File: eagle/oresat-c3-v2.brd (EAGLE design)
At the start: 99.8 x 94.7 mm, 168 parts, among them J1 J-SAMTEC-TFM-110-X1-XXX-D-RA, J10 U.FL, J11 U.FL, J13 U.FL, J14 U.FL, J15 HARWIN-2X8X1.27, J19 HARWIN-2X8X1.27, J2 U.FL, J3 U.FL, J4 U.FL, J6 J-SAMTEC-TFM-120-X1-XXX-D-RA, J7 FTSH-105-XX-X-DV-K, J8 U.FL, J9 U.FL, Q1 MOSFET-PCH-SOT23-6, U1 MAX892LEUA+T21-0036K-L, U11 U-ONSEMI-AX5043, U12 LP2985XX-N, U13 U-ONSEMI-AX5043, U14 LP2985XX-N, U2 TCAN330, U3 TCAN330, U4 TPS259621 - eFuse, U5 TPS62111RSA, U6 MAX6374KA-T21-0078H-L, U7 STM32F446RE, U9 SFEM016GB1EM1TO-A-HG-111-STD, X1 16MHZ-2.5x2mm, X3 TAITIEN-TY, X4 TAITIEN-TY

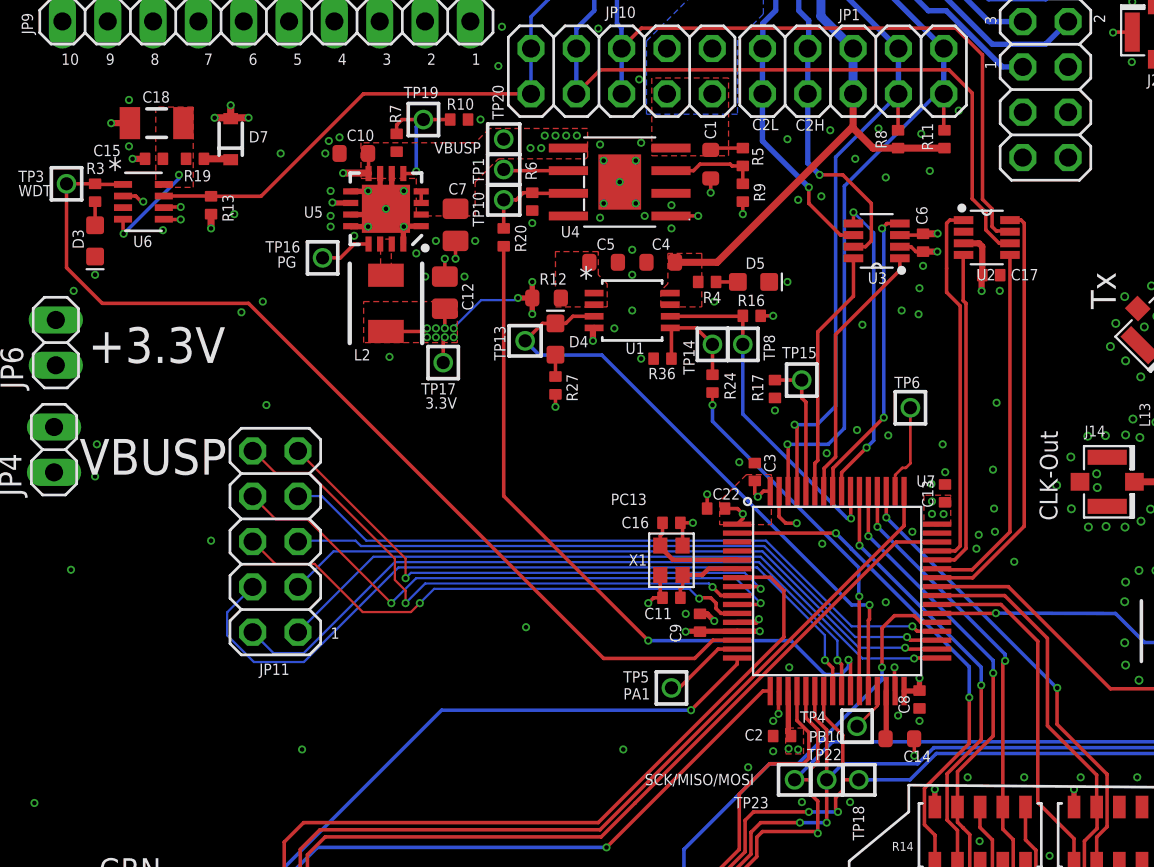
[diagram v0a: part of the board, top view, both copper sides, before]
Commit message: Replacing non 0603 with 0603 package equivalents
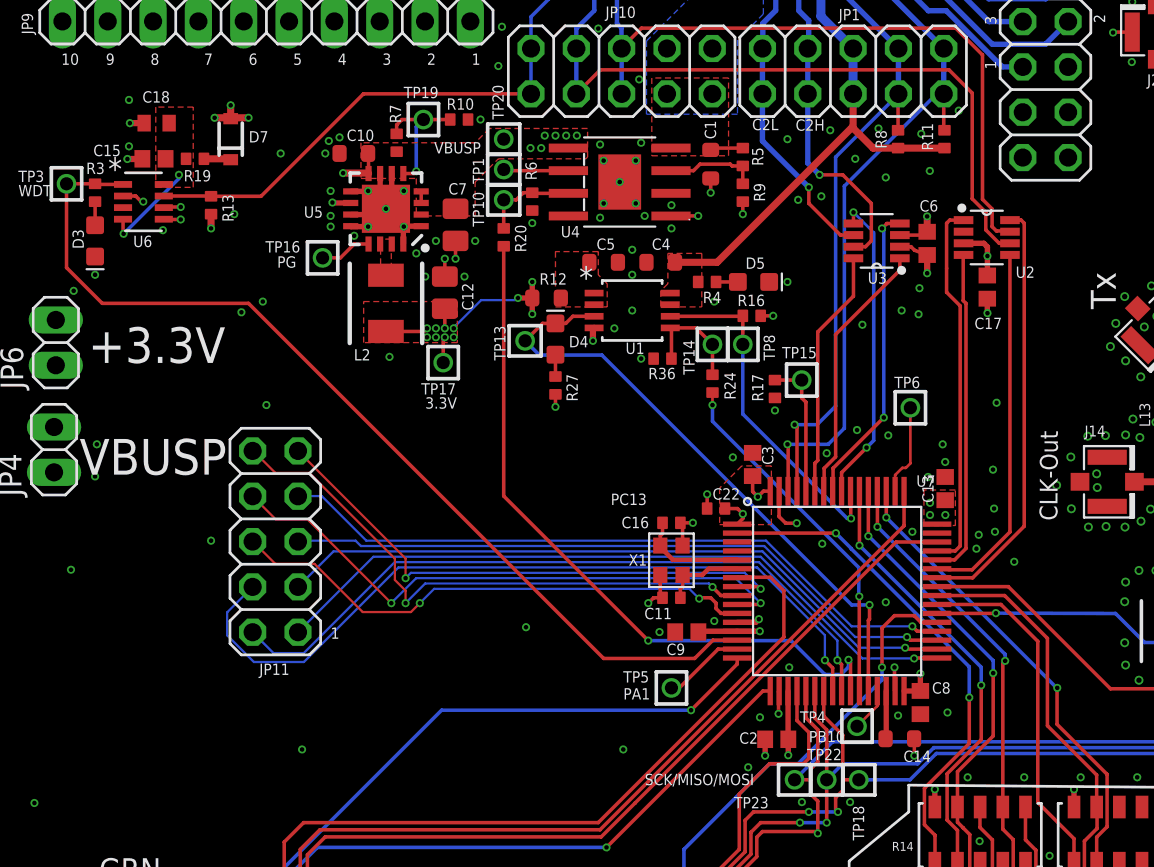
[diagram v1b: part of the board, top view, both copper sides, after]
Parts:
- C13, C15, C17, C2, C3, C6, C8, C9: device oresat-rcl:.0402-B-NOSILK -> SamacSys_Parts:CAPC1608X95N
- C18: device oresat-rcl:1206-B -> SamacSys_Parts:CAPC1608X90N
- moved C9 0.90 mm to (45.6, 48.6), turned to 0 degrees
- moved C17 0.71 mm to (62.4, 67.9), turned to 90 degrees
- moved C3 0.44 mm to (49.2, 58.0)
- moved C2 0.35 mm to (50.6, 42.6)
- moved C13 0.27 mm to (60.0, 56.6)
- moved C6 0.23 mm to (59.0, 70.4)
- moved C8 0.18 mm to (58.6, 44.6)
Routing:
- net GND: track 107.0 -> 108.2 mm, vias 507 -> 506
- net 3.3V: track 56.9 -> 57.6 mm, vias 45 -> 43

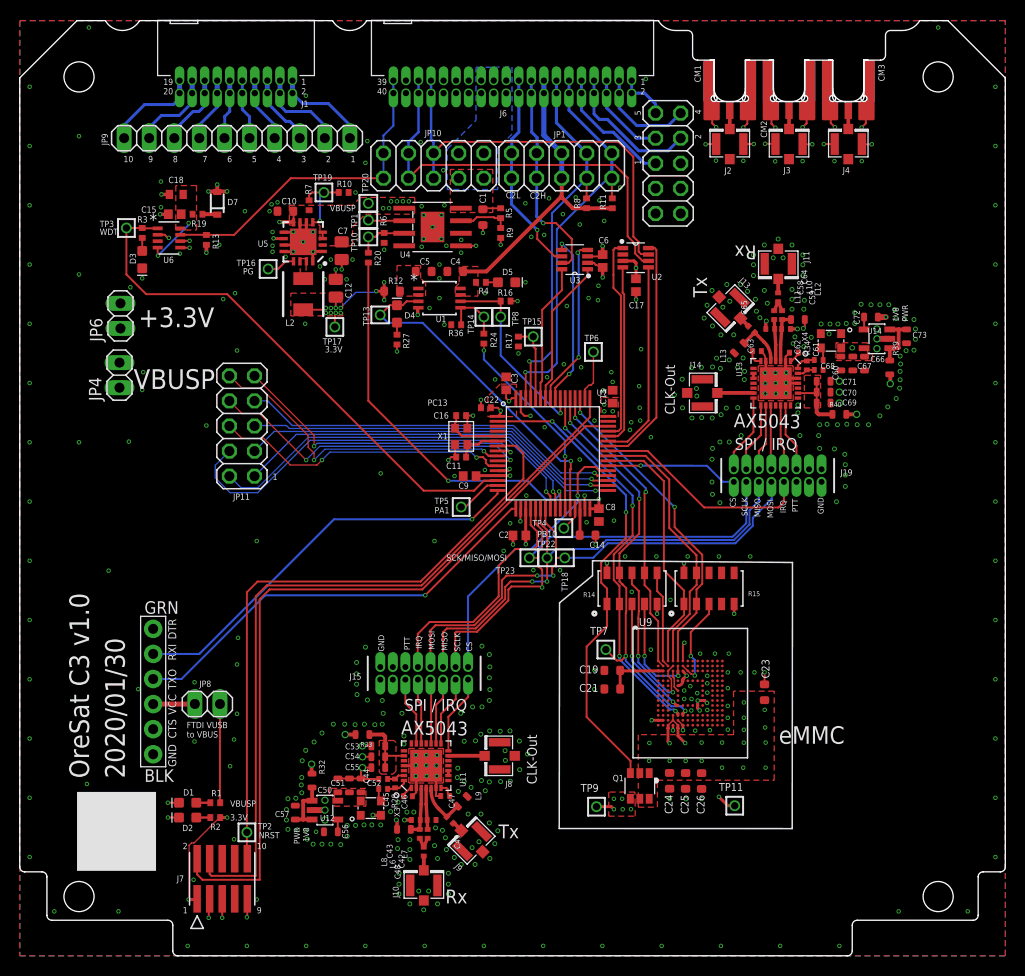
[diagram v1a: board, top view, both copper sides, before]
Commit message: Replaced non 0603 passive components with available 0603 equivalents
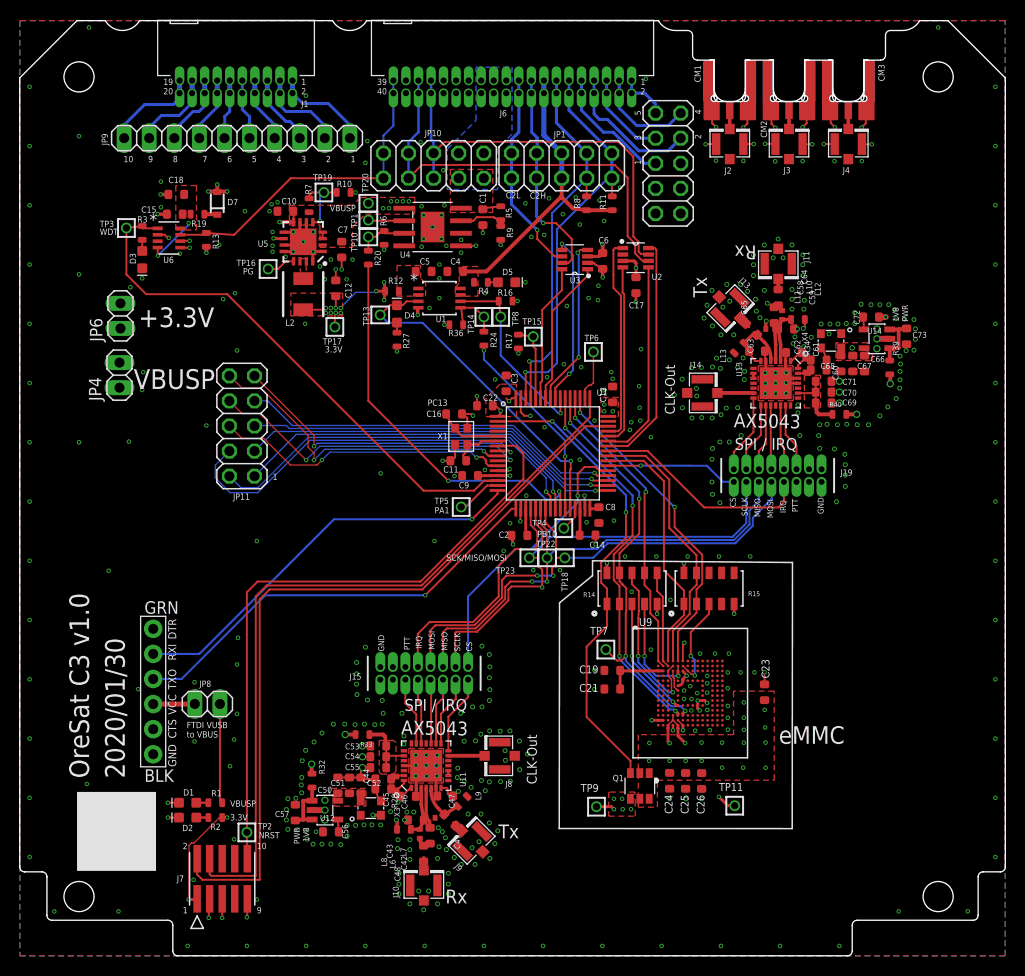
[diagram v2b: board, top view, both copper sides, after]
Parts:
- C1, C23, C24, C25, C4, C5: value 1u -> 1uF; device oresat-rcl:.0603-B-NOSILK -> C3_SamacSys_Parts:.0603-B-NOSILK
- C10: value 1u -> 10uF; device oresat-rcl:.0603-B-NOSILK -> C3_SamacSys_Parts:.0603-B-NOSILK
- C11: value 20p -> 20pF; device rcl_custom:.0402-B-NOSILK -> C3_SamacSys_Parts:.0603-B-NOSILK
- C12: value 22u -> 22pF; device oresat-rcl:.0805-B-NOSILK -> C3_SamacSys_Parts:.0603-B-NOSILK
- C13, C15, C17, C2, C3, C6, C8, C9: value 100n -> 0.1uf; device SamacSys_Parts:CAPC1608X95N -> C3_SamacSys_Parts:.0603-B-NOSILK
- C14: value 2.2u -> 2.2uF; device oresat-rcl:.0603-B-NOSILK -> C3_SamacSys_Parts:.0603-B-NOSILK
- C16: value 20p -> 20pF; device oresat-rcl:.0402-B-NOSILK -> C3_SamacSys_Parts:.0603-B-NOSILK
- C18: value 47u -> 47uF; device SamacSys_Parts:CAPC1608X90N -> C3_SamacSys_Parts:.0603-B-NOSILK
- C19, C26: device oresat-rcl:.0603-B-NOSILK -> C3_SamacSys_Parts:.0603-B-NOSILK
- C21: value 0.1u -> 0.1uf; device oresat-rcl:.0603-B-NOSILK -> C3_SamacSys_Parts:.0603-B-NOSILK
- C22: value 100n -> 0.1uf; device oresat-rcl:.0402-B-NOSILK -> C3_SamacSys_Parts:.0603-B-NOSILK
- C42, C43, C58, C59: value 8.2p -> 8.2pF; device oresat-rcl:.0402-C-NOSILK -> C3_SamacSys_Parts:.0603-B-NOSILK
- C44, C45, C60, C61: value 1n -> 1000pF; device oresat-rcl:.0402-C-NOSILK -> C3_SamacSys_Parts:.0603-B-NOSILK
- C46, C47, C62, C63: value 82p -> 82pF; device oresat-rcl:.0402-C-NOSILK -> C3_SamacSys_Parts:.0603-B-NOSILK
- C48, C49, C64, C65: value 22p -> 22pF; device oresat-rcl:.0402-C-NOSILK -> C3_SamacSys_Parts:.0603-B-NOSILK
- C50, C53, C66, C69: value 22n -> 0.022uF; device oresat-rcl:.0603-C-NOSILK -> C3_SamacSys_Parts:.0603-B-NOSILK
- C51, C54: value NP -> 0.022uF; device oresat-rcl:.0603-C-NOSILK -> C3_SamacSys_Parts:.0603-B-NOSILK
- C52, C55, C68, C71: value 4.7u -> 4.7uF; device oresat-rcl:.0603-C-NOSILK -> C3_SamacSys_Parts:.0603-B-NOSILK
- C56, C72: device oresat-rcl:.0603-C-NOSILK -> C3_SamacSys_Parts:.0603-B-NOSILK
- C57, C73: value 1u -> 1uF; device oresat-rcl:.0603-C-NOSILK -> C3_SamacSys_Parts:.0603-B-NOSILK
- C67, C70: value NP -> 0.1uf; device oresat-rcl:.0603-C-NOSILK -> C3_SamacSys_Parts:.0603-B-NOSILK
- C7: value 10u -> 10uF; device oresat-rcl:.0805-B-NOSILK -> C3_SamacSys_Parts:.0603-B-NOSILK
- R1, R10, R11, R13, R16, R17, R19, R2, R20, R24, R27, R3, R4, R6, R7, R8, R9: device oresat-rcl:.0402-B-NOSILK -> C3_SamacSys_Parts:.0603-C-NOSILK
- R12: device oresat-rcl:.0603-B-NOSILK -> C3_SamacSys_Parts:.0603-C-NOSILK
- R28, R34: device oresat-rcl:.0402-C-NOSILK -> C3_SamacSys_Parts:.0603-C-NOSILK
- R32, R33, R39, R40: device oresat-rcl:.0603-C-NOSILK -> C3_SamacSys_Parts:.0603-C-NOSILK
- R36: value 23.9k -> 23.7k; device oresat-rcl:.0402-B-NOSILK -> C3_SamacSys_Parts:.0603-C-NOSILK
- R5: value 31.7k -> 31.6k; device oresat-rcl:.0402-B-NOSILK -> C3_SamacSys_Parts:.0603-C-NOSILK
- moved C16 0.74 mm to (44.0, 54.9)
- moved C11 0.47 mm to (44.4, 50.1)
- moved C42 0.31 mm to (41.6, 12.2)
- moved L7 0.24 mm to (41.6, 14.0)
- moved C13 0.23 mm to (60.0, 56.9)
- moved C22 0.22 mm to (47.1, 55.7)
- moved C48 0.21 mm to (40.9, 10.3)
- moved C7 0.12 mm to (32.6, 71.5)
- moved C9 0.06 mm to (45.6, 48.6)
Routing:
- net 3.3V: track 57.6 -> 54.1 mm, vias 43 -> 41
- net N$17: track 1.97 -> 1.13 mm
- net CRYSTALOUT: track 4.53 -> 5.13 mm

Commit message: Parts Move so far
not completed
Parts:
- removed JP11, JP2: (no value), pinhead:2X05
- removed JP4, JP6: (no value), J-2X8X1.27:1X02
- removed TP9: TEST-POINT, Tova:2MM-TEST-POINT
- moved TP11 72.5 mm to (7.29, 47.1)
- moved C26 67.7 mm to (9.10, 49.1), turned to 180 degrees
- moved C25 67.0 mm to (9.11, 50.7), turned to 180 degrees
- moved C24 66.4 mm to (9.12, 52.4), turned to 180 degrees
- moved C23 59.5 mm to (18.1, 42.8), turned to 0 degrees
- moved D2 58.0 mm to (20.0, 71.9)
- moved R2 58.0 mm to (22.8, 71.9)
- moved D1 57.9 mm to (20.1, 73.3)
- moved R1 57.9 mm to (22.9, 73.3)
- moved U9 55.2 mm to (18.0, 50.3), turned to 270 degrees
- moved Q1 54.9 mm to (13.9, 42.1), turned to 270 degrees
- moved C21 52.0 mm to (18.4, 58.2), turned to 90 degrees
- moved C19 49.3 mm to (20.3, 58.2), turned to 90 degrees
- moved TP7 47.7 mm to (22.1, 60.7)
- moved R15 42.7 mm to (28.6, 48.4), turned to 0 degrees
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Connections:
- net !SD renamed SD
- removed net SPARE1: J6.10, J6.9, JP2.5
- removed net SPARE2: J6.7, J6.8, JP2.4
- removed net SPARE3: J6.5, J6.6, JP2.3
- removed net SPARE4: J6.3, J6.4, JP2.2
- removed net SPARE5: J6.1, J6.2, JP2.1
- net 3.3V: no longer JP6.1, JP6.2, TP9.1
- net GND: no longer JP2.10, JP2.7, JP2.8, JP2.9
- net MMC_PWR: now also R15.6; no longer R14.1
- net PB12: no longer JP11.1
- net PC0: no longer JP11.9
- net PC1: no longer JP11.10
- net PC2: no longer JP11.8
- net PC3: no longer JP11.6
- net PC4: no longer JP11.4
- net PC5: no longer JP11.2
- net SDIO_CK: now also R14.2; no longer R14.9
- net SDIO_CMD: now also R14.9; no longer R14.2
- net SPI2_MISO: no longer JP11.5
- net SPI2_MOSI: no longer JP11.7
- net SPI2_SCK: no longer JP11.3
- net VBUSP: no longer JP4.1, JP4.2
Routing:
- net VBUSP: track 74.5 -> 1.95 mm, vias 7 -> 6
- net SWCLK: track 77.9 -> 22.2 mm, vias 0 -> 2
- net SWDIO: track 79.1 -> 27.5 mm, vias 0 -> 2
- net NRST: track 65.3 -> 14.9 mm, vias 0 -> 2
- net PC4: track 44.5 -> 0.00 mm, vias 1 -> 0
- net USART2_RX: track 43.9 -> 0.00 mm, vias 1 -> 0
- net SPI1_MOSI: track 53.6 -> 10.9 mm, vias 2 -> 0
- net USART2_TX: track 41.9 -> 0.00 mm, vias 1 -> 0
- net SPI1_MISO: track 51.2 -> 10.6 mm, vias 2 -> 0
- net SPI1_SCK: track 51.9 -> 11.5 mm, vias 1 -> 0
- net PC5: track 40.1 -> 0.00 mm, vias 1 -> 0
- net PB12: track 39.9 -> 0.00 mm, vias 1 -> 0
- net CB_IOUT_IN: track 39.7 -> 0.00 mm, vias 2 -> 0
- net SPI2_MOSI: track 39.0 -> 0.00 mm, vias 1 -> 0
- net SPI2_SCK: track 38.9 -> 0.00 mm, vias 1 -> 0
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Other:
- board text added: "BOOT0"
- board text added: "SDIO_CK"
- board text removed: "+3.3V"
- board text removed: "PC13"
- board text removed: "SCK/MISO/MOSI"

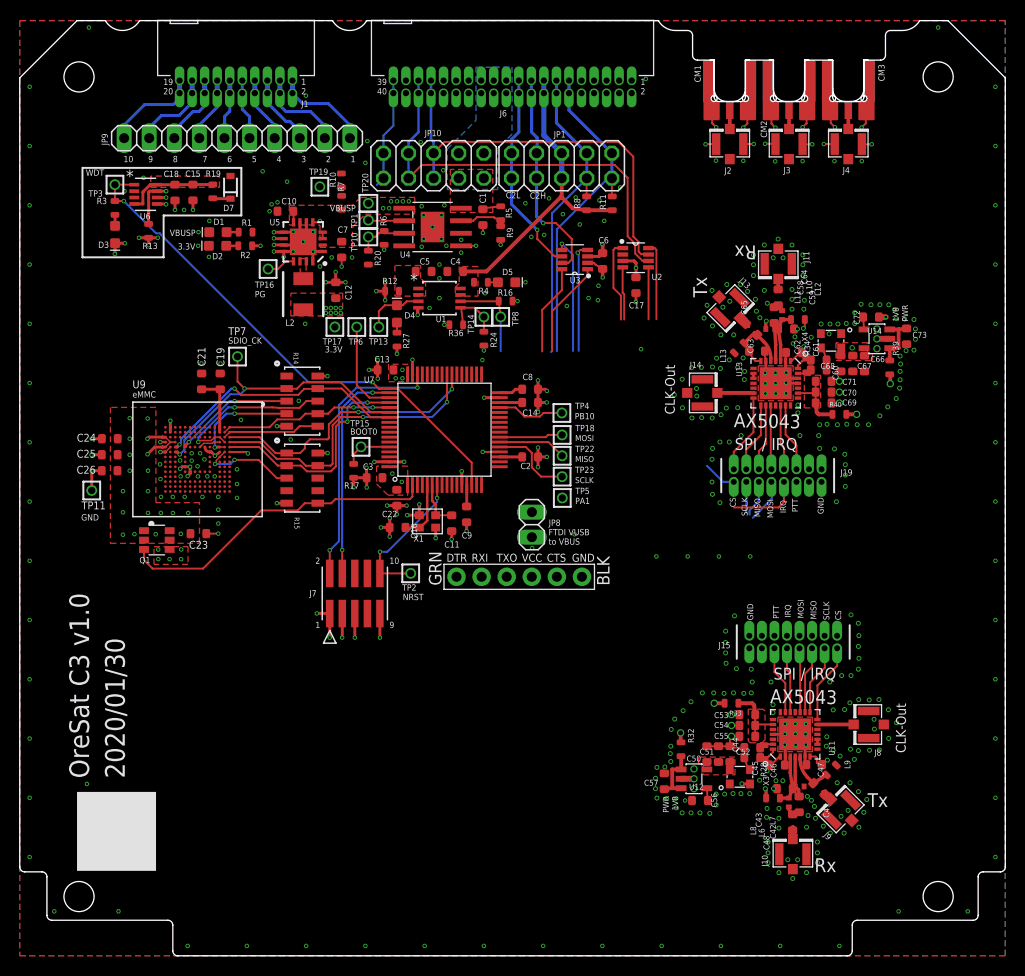
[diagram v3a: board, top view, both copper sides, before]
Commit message: Removed Jumpers and moved eMMC, processor, and more
Mostly reconnected , made changed to some of the polygons
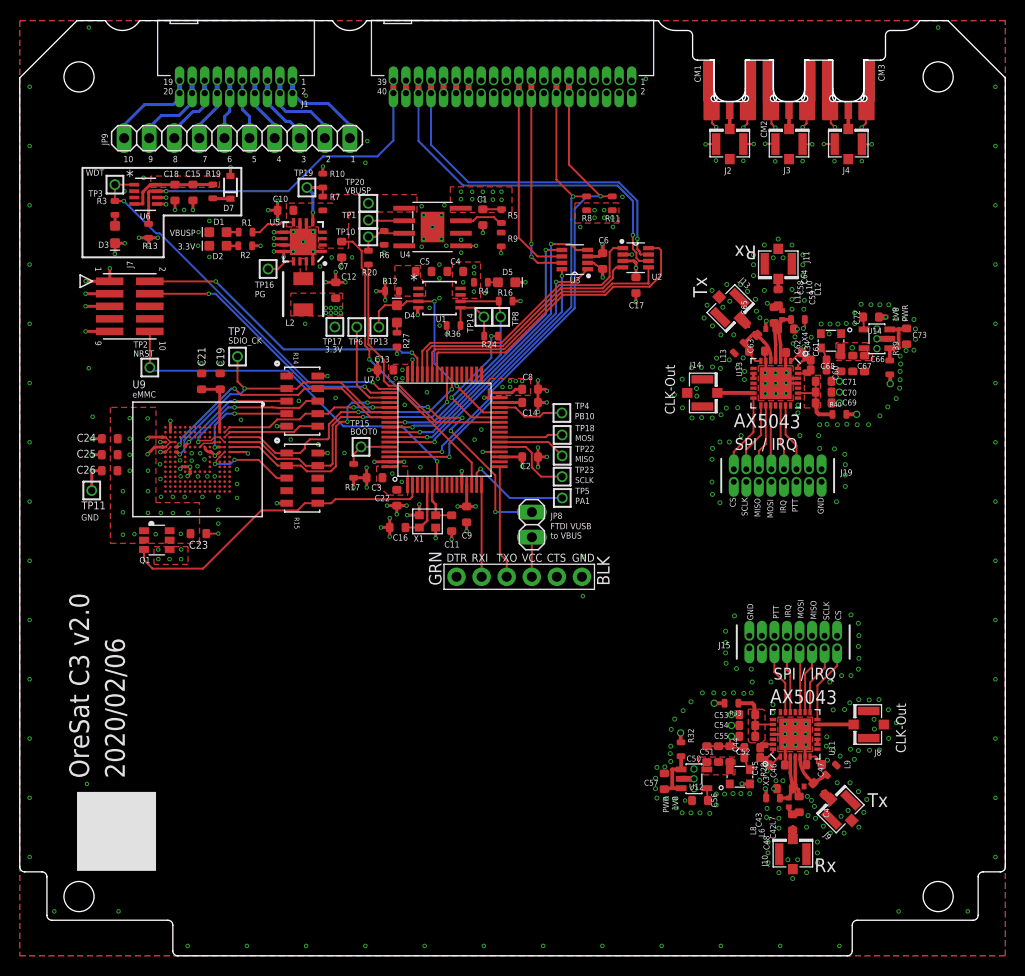
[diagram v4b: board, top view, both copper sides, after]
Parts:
- removed JP1, JP10: (no value), pinhead:2X05
- moved J7 36.9 mm to (11.1, 65.8), turned to 270 degrees
- moved TP2 33.6 mm to (13.2, 59.6)
- moved R7 1.90 mm to (30.7, 76.2)
- moved R10 1.88 mm to (30.7, 78.5)
- moved TP19 1.31 mm to (29.1, 77.8)
- moved R24 0.77 mm to (47.7, 62.8), turned to 0 degrees
- moved R9 0.66 mm to (48.8, 72.5)
- moved R5 0.30 mm to (48.8, 74.9)
- moved R36 0.28 mm to (43.9, 63.8)
- moved C10 0.09 mm to (26.9, 75.5)
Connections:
- net CAN1_H: no longer JP10.5, JP10.6
- net CAN1_L: no longer JP10.7, JP10.8
- net CAN2_H: no longer JP1.7, JP1.8
- net CAN2_L: no longer JP1.10, JP1.9
- net OPD_PWR: no longer JP1.5, JP1.6
- net OPD_SCL: no longer JP1.3, JP1.4
- net OPD_SDA: no longer JP1.1, JP1.2
- net SD: no longer JP10.10, JP10.9
- net VBUS: no longer JP10.1, JP10.2, JP10.3, JP10.4
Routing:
- net VBUSP: track 1.95 -> 45.7 mm, vias 6 -> 5
- net CB_IOUT_IN: track 0.00 -> 25.9 mm
- net NRST: track 14.9 -> 39.1 mm, vias 2 -> 1
- net CAN1_SILENT: track 7.90 -> 32.0 mm
- net CAN1_SHDN: track 5.26 -> 28.7 mm
- net CAN2_RX: track 11.1 -> 32.3 mm, vias 1 -> 2
- net CAN1_RX: track 5.36 -> 26.1 mm
- net OPD_SDA: track 33.9 -> 54.0 mm, vias 0 -> 2
- net CAN1_TX: track 8.41 -> 28.5 mm
- net SD: track 16.3 -> 36.2 mm
- net CAN2_TX: track 9.80 -> 29.0 mm, vias 0 -> 2
- net OPD_SCL: track 32.1 -> 50.5 mm, vias 0 -> 2
- net CAN2_SILENT: track 9.16 -> 27.4 mm, vias 0 -> 2
- net CAN2_SHDN: track 11.9 -> 28.7 mm, vias 1 -> 2
- net !OPD_ENABLE: track 6.02 -> 22.6 mm, vias 0 -> 2
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- added copper zone on layer 15, net OPD_PWR
- added copper zone on layer 15, net VBUS
- removed copper zone on layer 16, net VBUS
- removed copper zone on layer 15, net VBUSP
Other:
- board text added: "2020/02/06"
- board text added: "OreSat C3 v2.0"
- board text removed: "2020/01/30"
- board text removed: "C2H"
- board text removed: "C2L"
- board text removed: "OreSat C3 v1.0"
